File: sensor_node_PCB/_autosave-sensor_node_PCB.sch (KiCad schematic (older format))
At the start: 32 parts, among them J1 USB_B_Mini, J3 OUTPUT_CONNECTOR, P1 BREAKOUTS, Q1 FDN340P, Q2 BSS138, Q3 BSS138, U1 LMV358IDGKR, U2 LD1117S50TR, U3 FT231XS, U4 LM1117-3.3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

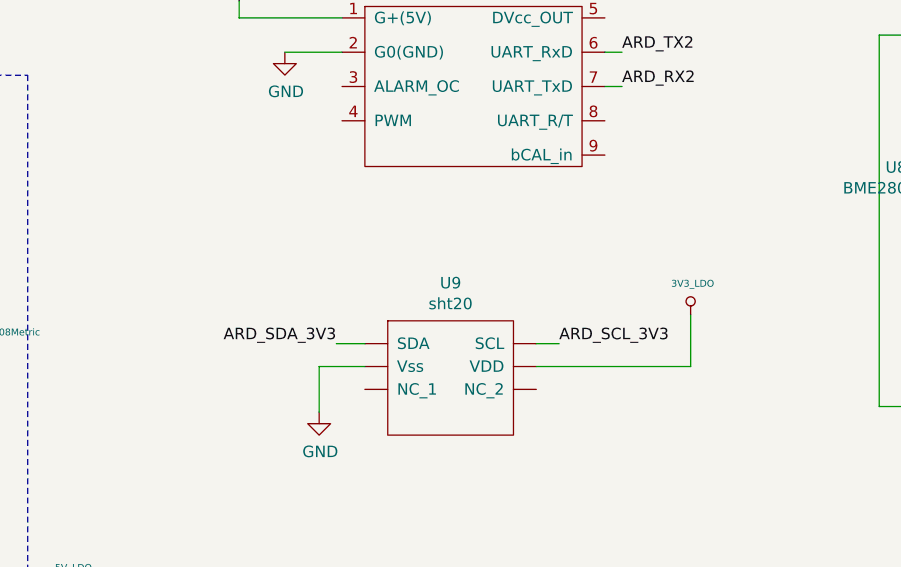
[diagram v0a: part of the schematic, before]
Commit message: added sht20 to tab
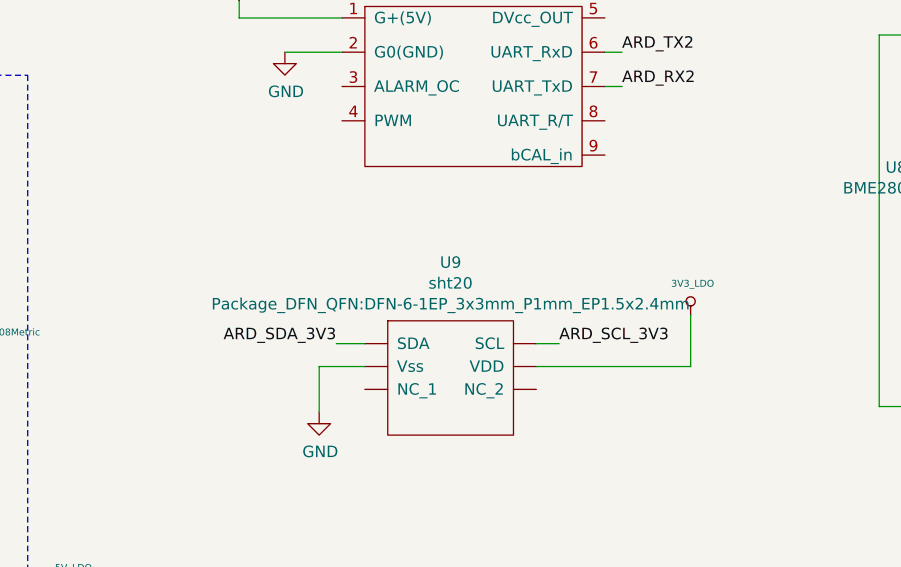
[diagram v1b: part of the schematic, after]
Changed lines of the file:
@@
 U 1 1 5FE5F04C
 P 7175 5275
-F 0 "U9" H 7000 5490 50  0000 C CNN
-F 1 "sht20" H 7000 5399 50  0000 C CNN
-F 2 "Package_DFN_QFN:DFN-6-1EP_3x3mm_P1mm_EP1.5x2.4mm" H 7175 5275 50  0001 C CNN
+F 0 "U9" H 7000 5580 50  0000 C CNN
+F 1 "sht20" H 7000 5489 50  0000 C CNN
+F 2 "Package_DFN_QFN:DFN-6-1EP_3x3mm_P1mm_EP1.5x2.4mm" H 7000 5398 50  0000 C CNN
 F 3 "" H 7175 5275 50  0001 C CNN
 	1    7175 5275
